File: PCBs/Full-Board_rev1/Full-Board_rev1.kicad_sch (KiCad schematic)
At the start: 1 part, among them U1 TPS630250RNCT

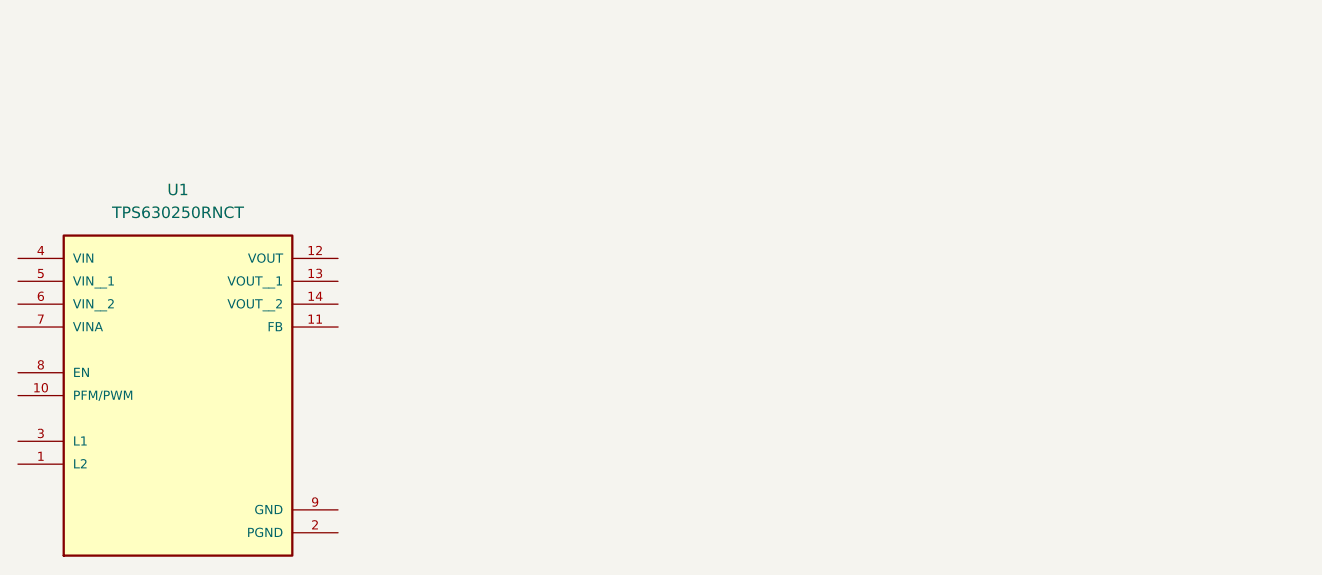
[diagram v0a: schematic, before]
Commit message: DC-DC base schematic created
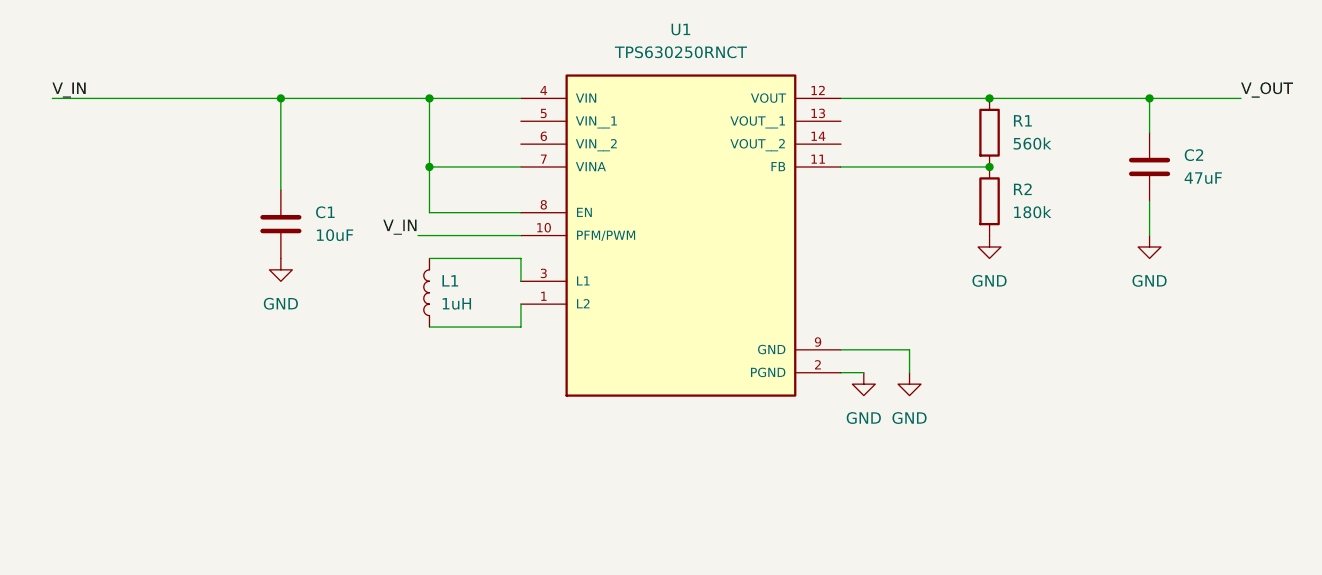
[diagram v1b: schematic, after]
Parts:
- added C1: 10uF, symbol Device:C
- added C2: 47uF, symbol Device:C
- added L1: 1uH, symbol Device:L
- added R1: 560k, symbol Device:R
- added R2: 180k, symbol Device:R
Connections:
- net at U1.1 (L2): now also L1.1
- net V_IN: now reaches U1.10 (PFM/PWM)
- net V_IN: now also U1.4 (VIN), U1.7 (VINA), U1.8 (EN), C1.1
- net at U1.11 (FB): now also R1.2, R2.1
- net V_OUT: now reaches U1.12 (VOUT)
- net V_OUT: now also C2.1, R1.1
- net GND: now reaches U1.2 (PGND)
- net GND: now also U1.9 (GND), C1.2, C2.2, R2.2
- net at U1.3 (L1): now also L1.2
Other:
- moved on the sheet: U1

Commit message: added modular design
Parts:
- removed C1: 10uF, symbol Device:C
- removed C2: 47uF, symbol Device:C
- removed L1: 1uH, symbol Device:L
- removed R1: 560k, symbol Device:R
- removed R2: 180k, symbol Device:R
- removed U1: TPS630250RNCT, TPS630250RNCT:VREG_TPS630250RNCT, symbol TPS630250RNCT:TPS630250RNCT
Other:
- added sheet 3v3_Regulator (3v3_Regulator.kicad_sch)
- title: (none) -> SwarmSolve PCB

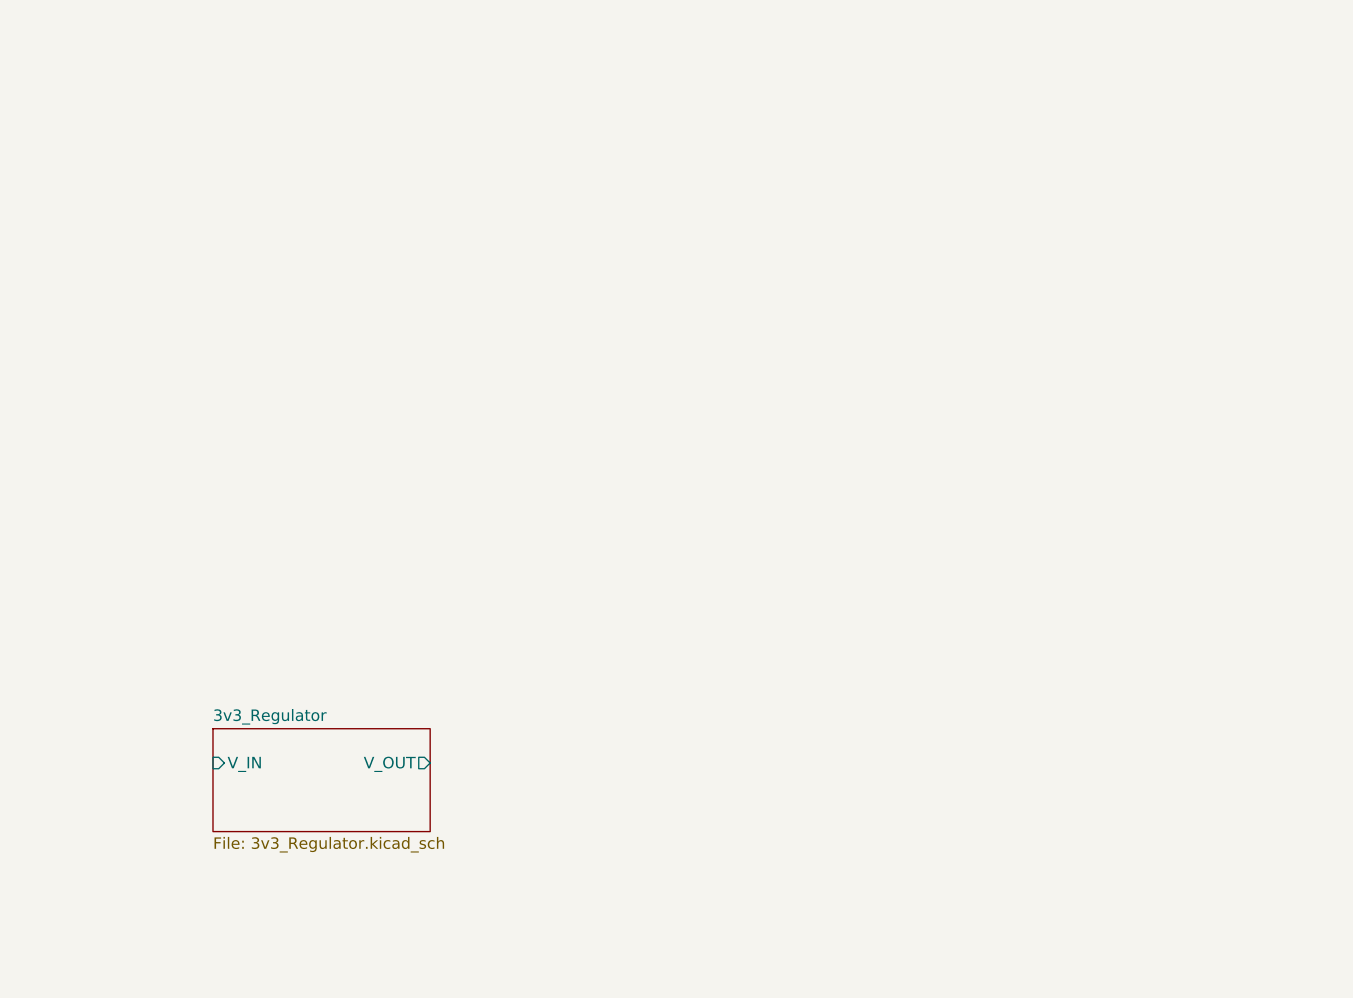
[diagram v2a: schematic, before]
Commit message: buttons and esp32 added
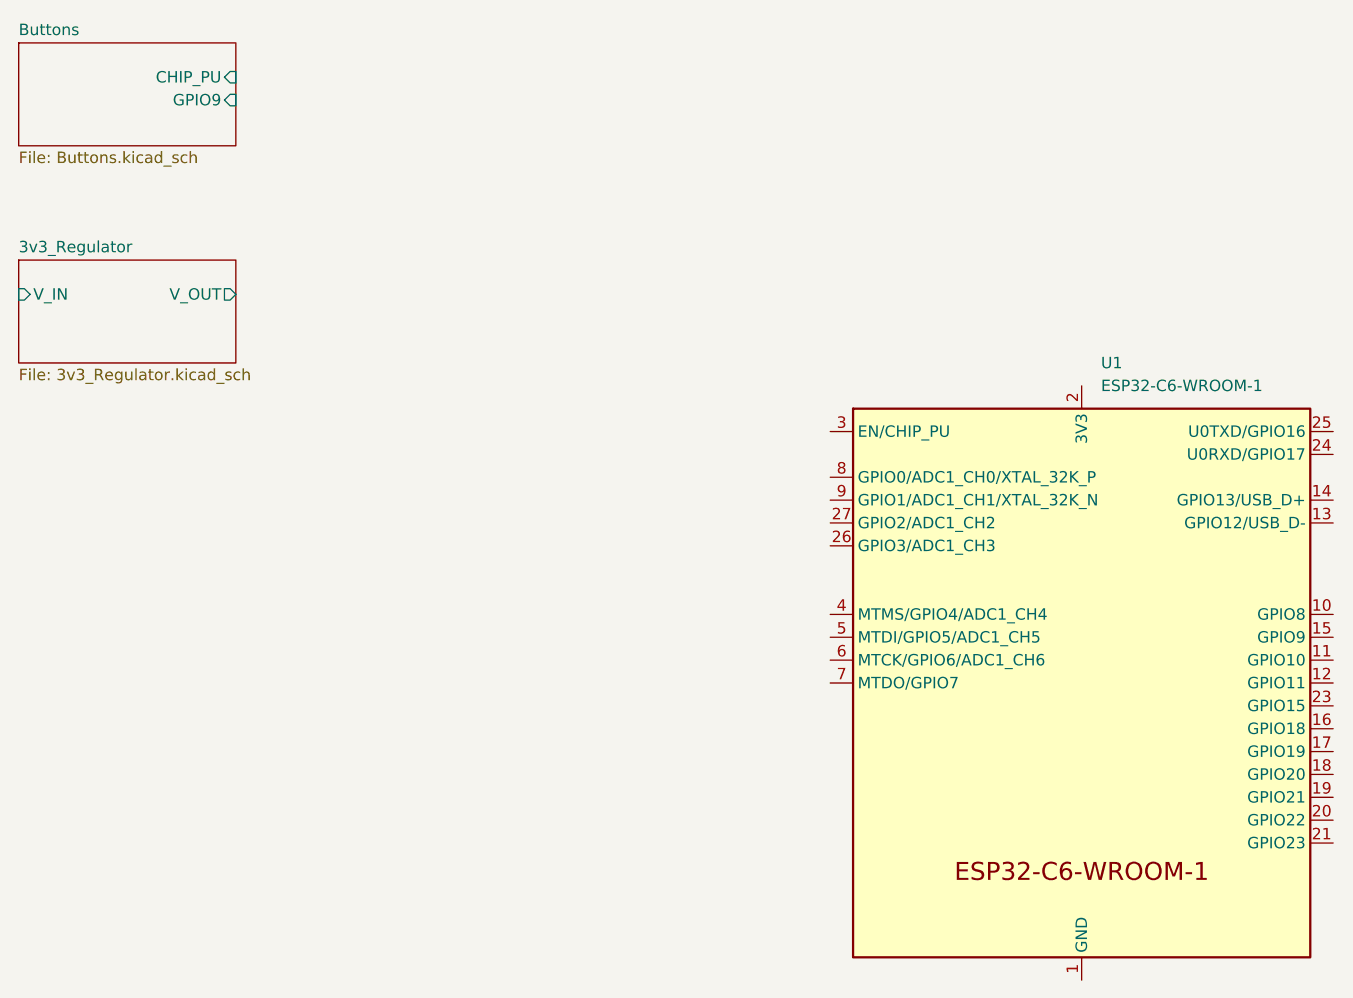
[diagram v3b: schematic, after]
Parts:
- added U1: ESP32-C6-WROOM-1, PCM_Espressif:ESP32-C6-WROOM-1, symbol Espressif:ESP32-C6-WROOM-1
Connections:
- new net: U1.1 (GND), U1.28 (GND), U1.29 (GND)
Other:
- added sheet Buttons (Buttons.kicad_sch)
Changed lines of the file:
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@@
 		(rev "1")
 	)
+	(symbol
+		(lib_id "Espressif:ESP32-C6-WROOM-1")
+		(at 147.32 95.25 0)
+		(unit 1)
+		(exclude_from_sim no)
+		(in_bom yes)
+		(on_board yes)
+		(dnp no)
+		(fields_autoplaced yes)
+		(property "Reference" "U1"
+			(at 149.4633 59.69 0)
+			(effects
+				(font
+					(size 1.27 1.27)
+				)
+				(justify left)
+			)
+		)
+		(property "Value" "ESP32-C6-WROOM-1"
+			(at 149.4633 62.23 0)
+			(effects
+				(font
+					(size 1.27 1.27)
+				)
+				(justify left)
+			)
+		)
+		(property "Footprint" "PCM_Espressif:ESP32-C6-WROOM-1"
+			(at 147.32 140.335 0)
+			(effects
+				(font
+					(size 1.27 1.27)
+				)
+				(hide yes)
+			)
+		)
+		(property "Datasheet" "https://www.espressif.com/sites/default/files/documentation/esp32-c6-wroom-1_wroom-1u_datasheet_en.pdf"
+			(at 147.32 143.51 0)
+			(effects
+				(font
+					(size 1.27 1.27)
+				)
+				(hide yes)
+			)
+		)
+		(property "Description" "ESP32-C6-WROOM-1/U is a module that supports 2.4 GHz Wi-Fi 6 (802.11 ax), Bluetooth® 5 (LE), Zigbee and Thread (802.15.4)"
+			(at 147.32 95.25 0)
+			(effects
+				(font
+					(size 1.27 1.27)
+				)
+				(hide yes)
+			)
+		)
+		(pin "12"
+		)
+		(pin "17"
+		)
+		(pin "19"
+		)
+		(pin "29"
+		)
+		(pin "22"
+		)
+		(pin "5"
+		)
+		(pin "16"
+		)
+		(pin "8"
+		)
+		(pin "9"
+		)
+		(pin "6"
+		)
+		(pin "28"
+		)
+		(pin "24"
+		)
+		(pin "4"
+		)
+		(pin "3"
+		)
+		(pin "14"
+		)
+		(pin "1"
+		)
+		(pin "25"
+		)
+		(pin "26"
+		)
+		(pin "13"
+		)
+		(pin "10"
+		)
+		(pin "27"
+		)
+		(pin "15"
+		)
+		(pin "7"
+		)
+		(pin "2"
+		)
+		(pin "11"
+		)
+		(pin "23"
+		)
+		(pin "18"
+		)
+		(pin "20"
+		)
+		(pin "21"
+		)
+		(instances
+			(project ""
+				(path "/2dd686ed-aa28-474a-bf3c-628eebb4b373"
+					(reference "U1")
+					(unit 1)
+				)
+			)
+		)
+	)
 	(sheet
-		(at 50.8 100.33)
+		(at 29.21 48.26)
 		(size 24.13 11.43)
 		(exclude_from_sim no)
@@
 		)
 		(property "Sheetname" "3v3_Regulator"
-			(at 50.8 99.6184 0)
+			(at 29.21 47.5484 0)
 			(effects
 				(font
@@
 		)
 		(property "Sheetfile" "3v3_Regulator.kicad_sch"
-			(at 50.8 112.3446 0)
+			(at 29.21 60.2746 0)
 			(effects
 				(font
@@
 		)
 		(pin "V_IN" input
-			(at 50.8 104.14 180)
+			(at 29.21 52.07 180)
 			(effects
 				(font
@@
 		)
 		(pin "V_OUT" output
-			(at 74.93 104.14 0)
+			(at 53.34 52.07 0)
 			(effects
 				(font
@@
 				)
 			)
+		)
+	)
+	(sheet
+		(at 29.21 24.13)
+		(size 24.13 11.43)
+		(exclude_from_sim no)
+		(in_bom yes)
+		(on_board yes)
+		(dnp no)
+		(fields_autoplaced yes)
+		(stroke
+			(width 0.1524)
+			(type solid)
+		)
+		(fill
+			(color 0 0 0 0.0000)
+		)
+		(property "Sheetname" "Buttons"
+			(at 29.21 23.4184 0)
+			(effects
+				(font
+					(size 1.27 1.27)
+				)
+				(justify left bottom)
+			)
+		)
+		(property "Sheetfile" "Buttons.kicad_sch"
+			(at 29.21 36.1446 0)
+			(effects
+				(font
+					(size 1.27 1.27)
+				)
+				(justify left top)
+			)
+		)
+		(pin "CHIP_PU" input
+			(at 53.34 27.94 0)
+			(effects
+				(font
+					(size 1.27 1.27)
+				)
+				(justify right)
+			)
+		)
+		(pin "GPIO9" input
+			(at 53.34 30.48 0)
+			(effects
+				(font
+					(size 1.27 1.27)
+				)
+				(justify right)
+			)
+		)
+		(instances
+			(project "Full-Board_rev1"
+				(path "/2dd686ed-aa28-474a-bf3c-628eebb4b373"
+					(page "3")
+				)
+			)

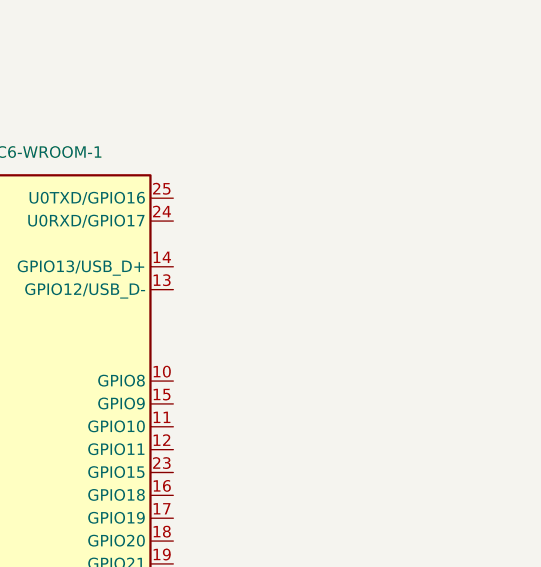
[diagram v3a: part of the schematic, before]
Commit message: Added USB-C
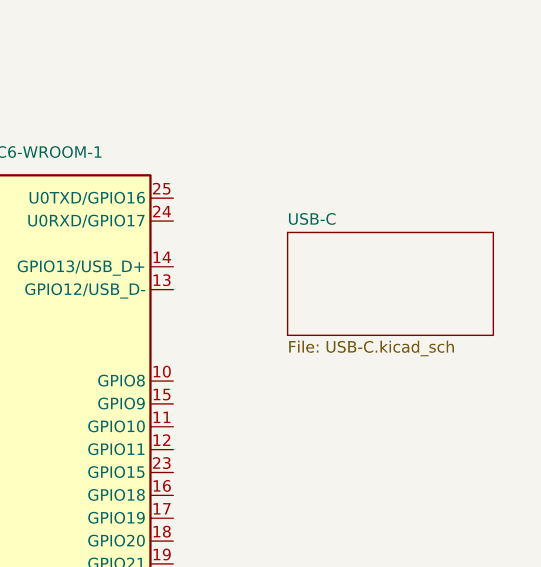
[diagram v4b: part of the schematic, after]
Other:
- added sheet USB-C (USB-C.kicad_sch)
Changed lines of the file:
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@@
+	)
+	(sheet
+		(at 187.96 71.12)
+		(size 22.86 11.43)
+		(exclude_from_sim no)
+		(in_bom yes)
+		(on_board yes)
+		(dnp no)
+		(fields_autoplaced yes)
+		(stroke
+			(width 0.1524)
+			(type solid)
+		)
+		(fill
+			(color 0 0 0 0.0000)
+		)
+		(property "Sheetname" "USB-C"
+			(at 187.96 70.4084 0)
+			(effects
+				(font
+					(size 1.27 1.27)
+				)
+				(justify left bottom)
+			)
+		)
+		(property "Sheetfile" "USB-C.kicad_sch"
+			(at 187.96 83.1346 0)
+			(effects
+				(font
+					(size 1.27 1.27)
+				)
+				(justify left top)
+			)
+		)
+		(instances
+			(project "Full-Board_rev1"
+				(path "/2dd686ed-aa28-474a-bf3c-628eebb4b373"
+					(page "4")
+				)
+			)
+		)
 	)
 	(sheet
